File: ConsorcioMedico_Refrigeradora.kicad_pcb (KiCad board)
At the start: 2 copper layers, 260 x 70 mm, 156 parts, among them J1 BatteryHolder, J10 AC, J11 Digital, J12 Light, J13 Light, J14 Compress, J15 Resistor, J16 Analog, J18 Resistor, J19 AC, J2 USART, J3 USART, J4 SWD, J5 Evap_fan, J6 Screw_Terminal_01x01, J7 Screw_Terminal_01x01, J8 Evap_fan, J9 Compress, K1 HF46F-G/012-HS1T, K2 AZ2150-1A-12DEF, K3 HF46F-G/012-HS1T, K4 HF46F-G/012-HS1T, Q1 MMBT3904, Q11 BSS806, Q2 MMBT3904, Q3 MMBT3904, Q4 MMBT3904, Q5 BSS806, Q6 BSS806, Q7 BSS806, Q8 BSS806, Q9 BSS806, U1 STM32F411RETx, U2 AP63205WU, U3 LDL1117, U4 INA350, U5 INA350, U6 LTV-357T, U7 LTV-357T, U9 HLK-PMx, Y1 8Mhz, Y2 32.768khz/12.5pF

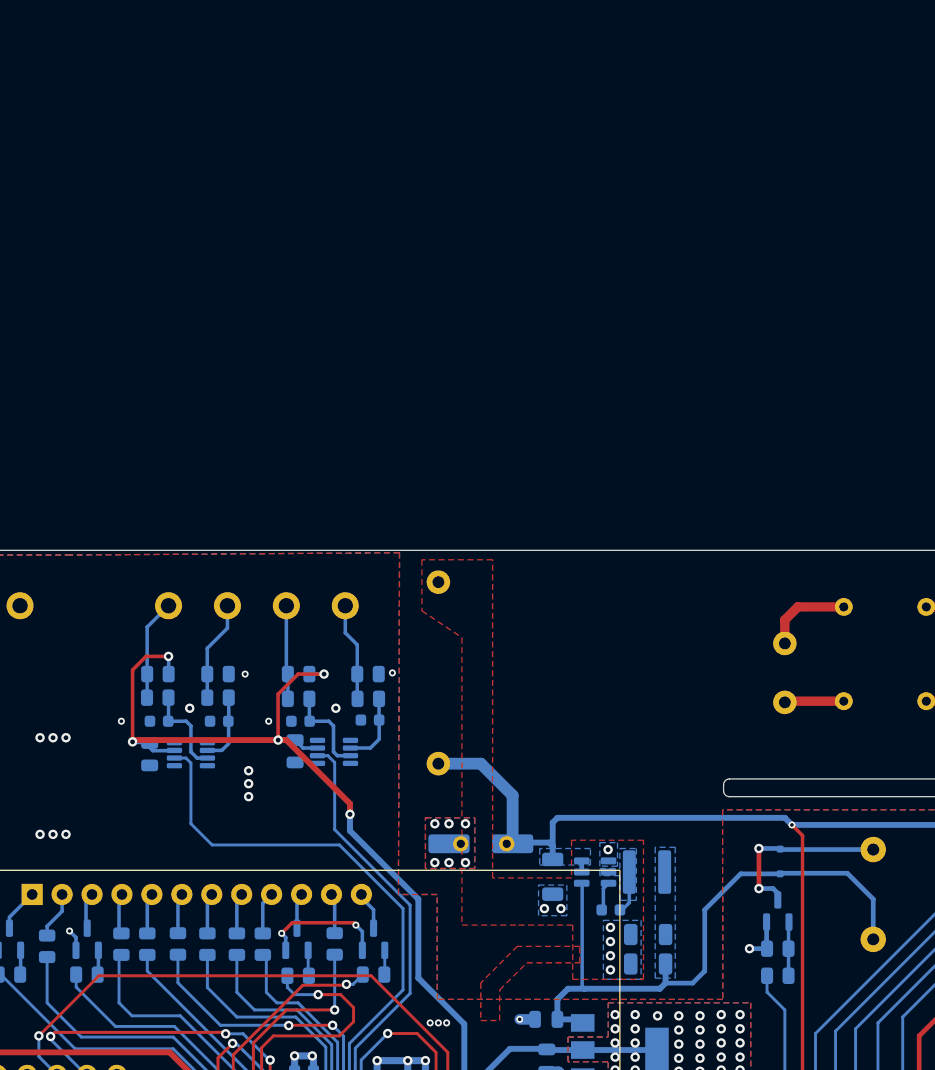
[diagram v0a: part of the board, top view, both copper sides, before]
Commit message: SCH:Se modifica los leds y nombres, en este punto, posibilemente se cambie el tamaño de la placa
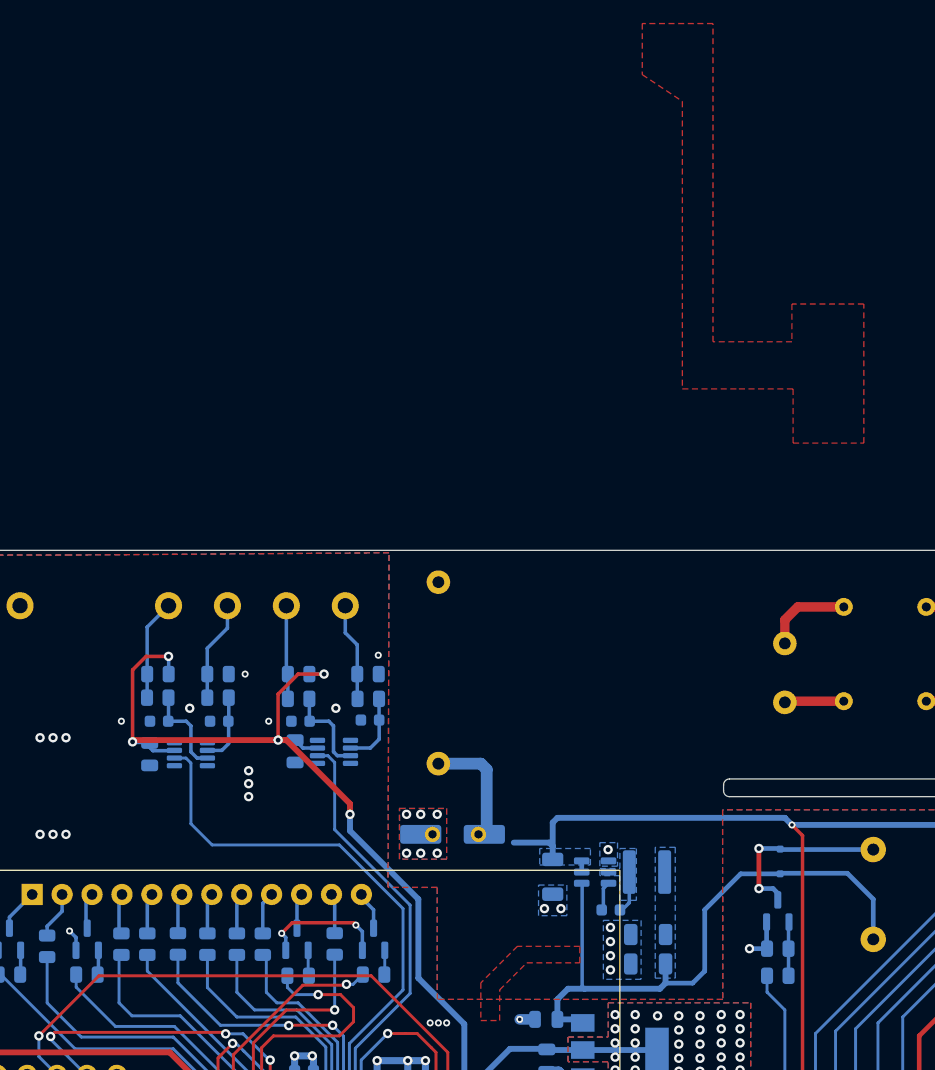
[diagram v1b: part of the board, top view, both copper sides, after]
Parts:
- moved J6 2.53 mm to (78.6, 87.7)
- moved C29 2.53 mm to (76.4, 87.7)
- moved J7 2.53 mm to (74.7, 87.7)
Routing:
- net +12V: track 410.1 -> 408.4 mm
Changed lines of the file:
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@@
   )
   (footprint "1-Pad:Pad_0.7mm_1.3mm" (layer "F.Cu")
-    (at 77.1 88.5)
+    (at 74.7 87.7)
     (property "Sheetfile" "ConsorcioMedico_Refrigeradora.kicad_sch")
     (property "Sheetname" "")
@@
   )
   (footprint "1-Pad:Pad_0.7mm_1.3mm" (layer "F.Cu")
-    (at 81 88.5)
+    (at 78.6 87.7)
     (property "Sheetfile" "ConsorcioMedico_Refrigeradora.kicad_sch")
     (property "Sheetname" "")
@@
   )
   (footprint "Capacitor_SMD:CP_Elec_6.3x7.7" (layer "B.Cu")
-    (at 78.8 88.5 180)
+    (at 76.4 87.7 180)
     (descr "SMD capacitor, aluminum electrolytic, Nichicon, 6.3x7.7mm")
     (tags "capacitor electrolytic")
@@
   (via (at 89.8 98) (size 0.8) (drill 0.4) (layers "F.Cu" "B.Cu") (net 2))
   (via (at 72.6 106.9) (size 0.8) (drill 0.4) (layers "F.Cu" "B.Cu") (net 2))
-  (via (at 77.5 90.1) (size 0.8) (drill 0.4) (layers "F.Cu" "B.Cu") (net 2))
+  (via (at 75.1 89.3) (size 0.8) (drill 0.4) (layers "F.Cu" "B.Cu") (net 2))
   (via (at 52.4 117.6) (size 0.6) (drill 0.3) (layers "F.Cu" "B.Cu") (net 2))
   (via (at 67.5 116.6) (size 0.6) (drill 0.3) (layers "F.Cu" "B.Cu") (net 2))
@@
   (via (at 174.6 83.4) (size 0.8) (drill 0.4) (layers "F.Cu" "B.Cu") (free) (net 2))
   (via (at 89.8 95.6) (size 0.8) (drill 0.4) (layers "F.Cu" "B.Cu") (net 2))
-  (via (at 74.9 90.1) (size 0.8) (drill 0.4) (layers "F.Cu" "B.Cu") (net 2))
+  (via (at 72.5 89.3) (size 0.8) (drill 0.4) (layers "F.Cu" "B.Cu") (net 2))
   (via (at 146.5 83.3) (size 0.8) (drill 0.4) (layers "F.Cu" "B.Cu") (free) (net 2))
-  (via (at 76.1 90.1) (size 0.8) (drill 0.4) (layers "F.Cu" "B.Cu") (net 2))
+  (via (at 73.7 89.3) (size 0.8) (drill 0.4) (layers "F.Cu" "B.Cu") (net 2))
   (via (at 122.6 126.1) (size 0.8) (drill 0.4) (layers "F.Cu" "B.Cu") (free) (net 2))
   (via (at 74.5 103.7) (size 0.6) (drill 0.3) (layers "F.Cu" "B.Cu") (free) (net 2))
@@
   (via (at 89.8 96.8) (size 0.8) (drill 0.4) (layers "F.Cu" "B.Cu") (net 2))
   (via (at 59.1 84.5) (size 0.8) (drill 0.4) (layers "F.Cu" "B.Cu") (free) (net 2))
-  (via (at 74.9 86.8) (size 0.8) (drill 0.4) (layers "F.Cu" "B.Cu") (net 2))
+  (via (at 72.5 86) (size 0.8) (drill 0.4) (layers "F.Cu" "B.Cu") (net 2))
   (via (at 63.1 110.3) (size 0.6) (drill 0.3) (layers "F.Cu" "B.Cu") (net 2))
   (via (at 75.2 103.7) (size 0.6) (drill 0.3) (layers "F.Cu" "B.Cu") (free) (net 2))
@@
   (via (at 80.9 127.5) (size 0.6) (drill 0.3) (layers "F.Cu" "B.Cu") (free) (net 2))
   (via (at 85.6 94) (size 0.8) (drill 0.4) (layers "F.Cu" "B.Cu") (net 2))
-  (via (at 71.3 74) (size 0.6) (drill 0.3) (layers "F.Cu" "B.Cu") (free) (net 2))
+  (via (at 70.1 72.5) (size 0.6) (drill 0.3) (layers "F.Cu" "B.Cu") (free) (net 2))
   (via (at 89.8 99.2) (size 0.8) (drill 0.4) (layers "F.Cu" "B.Cu") (net 2))
   (via (at 16.6 83.4) (size 0.8) (drill 0.4) (layers "F.Cu" "B.Cu") (free) (net 2))
@@
   (via (at 170.4 83.4) (size 0.8) (drill 0.4) (layers "F.Cu" "B.Cu") (free) (net 2))
   (via (at 212.2 83.3) (size 0.8) (drill 0.4) (layers "F.Cu" "B.Cu") (free) (net 2))
-  (via (at 76.1 86.8) (size 0.8) (drill 0.4) (layers "F.Cu" "B.Cu") (net 2))
+  (via (at 73.7 86) (size 0.8) (drill 0.4) (layers "F.Cu" "B.Cu") (net 2))
   (via (at 123.7 126.1) (size 0.8) (drill 0.4) (layers "F.Cu" "B.Cu") (free) (net 2))
   (via (at 54.1 77) (size 0.8) (drill 0.4) (layers "F.Cu" "B.Cu") (free) (net 2))
@@
   (via (at 132.5 114.6) (size 0.8) (drill 0.4) (layers "F.Cu" "B.Cu") (free) (net 2))
   (via (at 64.5 106.5) (size 0.8) (drill 0.4) (layers "F.Cu" "B.Cu") (net 2))
-  (via (at 77.5 86.8) (size 0.8) (drill 0.4) (layers "F.Cu" "B.Cu") (net 2))
+  (via (at 75.1 86) (size 0.8) (drill 0.4) (layers "F.Cu" "B.Cu") (net 2))
   (via (at 80.9 125.5) (size 0.6) (drill 0.3) (layers "F.Cu" "B.Cu") (free) (net 2))
   (via (at 59.1 83.4) (size 0.8) (drill 0.4) (layers "F.Cu" "B.Cu") (free) (net 2))
@@
   (via (at 166.5 86.5) (size 0.8) (drill 0.4) (layers "F.Cu" "B.Cu") (net 106))
   (segment (start 204.95 86.3) (end 204.95 84.45) (width 0.5) (layer "B.Cu") (net 106))
-  (segment (start 81.5 88.5) (end 81.5 84.4) (width 1) (layer "B.Cu") (net 106))
   (segment (start 204.95 84.45) (end 206.05 83.35) (width 0.5) (layer "B.Cu") (net 106))
   (segment (start 87.3625 90.9) (end 87.3625 89.95) (width 0.4) (layer "B.Cu") (net 106))
@@
   (segment (start 186.0875 86.0875) (end 186.5 86.5) (width 0.5) (layer "B.Cu") (net 106))
   (segment (start 218.35 88.95) (end 220.7 86.6) (width 0.5) (layer "B.Cu") (net 106))
-  (segment (start 81.5 84.4) (end 78.8 81.7) (width 1) (layer "B.Cu") (net 106))
   (segment (start 220.7 84.9) (end 222.235 83.365) (width 0.5) (layer "B.Cu") (net 106))
   (segment (start 105.2 86.9) (end 104.6 86.3) (width 0.5) (layer "B.Cu") (net 106))
@@
   (segment (start 165.05 85.05) (end 166.35 83.75) (width 0.5) (layer "B.Cu") (net 106))
   (segment (start 220.7 86.6) (end 220.7 84.9) (width 0.5) (layer "B.Cu") (net 106))
+  (segment (start 79.3 87.7) (end 79.3 82.2) (width 1) (layer "B.Cu") (net 106))
   (segment (start 186.25 83.35) (end 186.65 83.35) (width 0.5) (layer "B.Cu") (net 106))
   (segment (start 206 86.3) (end 206.2 86.5) (width 0.5) (layer "B.Cu") (net 106))
@@
   (segment (start 165.05 86.1125) (end 165.05 85.05) (width 0.5) (layer "B.Cu") (net 106))
   (segment (start 165.05 86.1125) (end 166.1125 86.1125) (width 0.5) (layer "B.Cu") (net 106))
-  (segment (start 81.6 88.4) (end 81.5 88.5) (width 0.5) (layer "B.Cu") (net 106))
+  (segment (start 79.2 87.6) (end 79.1 87.7) (width 0.5) (layer "B.Cu") (net 106))
   (segment (start 21.8 72.4) (end 20.6 73.6) (width 0.3) (layer "B.Cu") (net 106))
+  (segment (start 79.3 82.2) (end 78.8 81.7) (width 1) (layer "B.Cu") (net 106))
   (segment (start 217.6 90) (end 217.5 90.1) (width 0.5) (layer "B.Cu") (net 106))
   (segment (start 32.1125 66.1125) (end 31.3 65.3) (width 0.3) (layer "B.Cu") (net 106))
@@
     (polygon
       (pts
-        (xy 73.8 64.4)
-        (xy 73.8 68.733334)
-        (xy 77.2 71)
-        (xy 77.2 95.4)
-        (xy 82 95.4)
-        (xy 86.6 95.4)
-        (xy 86.6 100)
-        (xy 92.6 100)
-        (xy 92.6 88.2)
-        (xy 86.5 88.2)
-        (xy 86.5 91.4)
-        (xy 79.8 91.4)
-        (xy 79.8 64.4)
+        (xy 92.5 18.9)
+        (xy 92.5 23.233334)
+        (xy 95.9 25.5)
+        (xy 95.9 49.9)
+        (xy 100.7 49.9)
+        (xy 105.3 49.9)
+        (xy 105.3 54.5)
+        (xy 111.3 54.5)
+        (xy 111.3 42.7)
+        (xy 105.2 42.7)
+        (xy 105.2 45.9)
+        (xy 98.5 45.9)
+        (xy 98.5 18.9)
       )
     )
@@
     (connect_pads (clearance 0.3))
     (min_thickness 0.25) (filled_areas_thickness no)
-    (fill yes (thermal_gap 0.5) (thermal_bridge_width 0.5) (smoothing fillet) (radius 0.5))
+    (fill (thermal_gap 0.5) (thermal_bridge_width 0.5) (smoothing fillet) (radius 0.5))
     (polygon
       (pts
@@
         (xy 99.326686 101.703776)
         (xy 75.1 101.7)
-        (xy 75.1 92.8)
-        (xy 71.810467 92.8)
-        (xy 71.9 63.8)
+        (xy 75.1 92.2)
+        (xy 70.925283 92.2)
+        (xy 71.012944 63.806359)
         (xy 44 64)
       )
@@
     (connect_pads yes (clearance 0.3))
     (min_thickness 0.25) (filled_areas_thickness no)
-    (fill yes (thermal_gap 0.5) (thermal_bridge_width 0.5) (smoothing fillet) (radius 0.25))
+    (fill (thermal_gap 0.5) (thermal_bridge_width 0.5) (smoothing fillet) (radius 0.25))
     (polygon
       (pts
-        (xy 74.1 86.3)
-        (xy 78.3 86.3)
-        (xy 78.3 90.6)
-        (xy 74.1 90.6)
+        (xy 71.9 85.5)
+        (xy 75.9 85.5)
+        (xy 75.9 89.8)
+        (xy 71.9 89.8)
       )
     )

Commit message: SCH
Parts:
- added D13: Button_Lock, 1-Led:LED_3mm, F.Cu at (108.9, 104.6)
- added D14: Door_State, 1-Led:LED_3mm, F.Cu at (108.9, 117.2)
- added D3: Powe_State, 1-Led:LED_3mm, F.Cu at (108.9, 91.9)
- added R52: 560R, 1-Resistor:R_0805_2012Metric, B.Cu at (108.8, 95.3)
- added R58: 560R, 1-Resistor:R_0805_2012Metric, B.Cu at (109.0, 107.9)
- added R59: 560R, 1-Resistor:R_0805_2012Metric, B.Cu at (109.0, 113.7)
- D7: value L-144IDT -> Cooling_State; footprint 1-Led:LED_3.9x1.9mm -> 1-Led:LED_3mm
- D8: value L-144IDT -> Defroting_State; footprint 1-Led:LED_3.9x1.9mm -> 1-Led:LED_3mm
- D9: value L-144IDT -> Fan_State; footprint 1-Led:LED_3.9x1.9mm -> 1-Led:LED_3mm
- J3: value USART -> I2C
- R2, R4, R5: value 330 -> 560R
- moved C12 25.4 mm to (45.2, 122.4), turned to -90 degrees
- moved R16 22.2 mm to (152.4, 113.5), turned to 180 degrees
- moved S2 19.7 mm to (153.4, 110.8)
- moved R17 18.5 mm to (179.2, 113.5), turned to 180 degrees
- moved J1 17.7 mm to (41.2, 122.3), turned to 180 degrees
- moved S3 16.5 mm to (180.3, 110.8)
- moved R18 14.8 mm to (198.3, 113.5), turned to 180 degrees
- moved S4 11.6 mm to (199.3, 110.8)
- moved SG2 11.0 mm to (122.8, 95.5), turned to 90 degrees
- moved Q11 10.8 mm to (114.7, 95.5)
- moved R56 10.8 mm to (114.7, 101.0)
- moved R57 10.8 mm to (114.7, 98.7)
- moved D2 10.7 mm to (114.8, 91.5), turned to -90 degrees
- moved R15 9.48 mm to (217.8, 113.5), turned to 180 degrees
- moved R5 7.31 mm to (10.9, 120.5)
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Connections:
- net Button_Buzzer renamed Button_Power
- net Button_Touch renamed Button_Set
- net LED_Defrost renamed Led_Cooling_State
- net LED_Door renamed Led_Defroting_State
- net LED_Status renamed Led_Status
- net LED_TempAlarm renamed Led_Fan_State
- R19 pad 1: Button_Cooling -> Button_Light
- R20 pad 1: Button_Light -> Button_Sound
- S5 pad 1: Button_Cooling -> Button_Light
- S6 pad 1: Button_Light -> Button_Sound
- U1 pad 27: unconnected-(U1-PB1-Pad27) -> Led_Power_State
- U1 pad 28: unconnected-(U1-PB2-Pad28) -> Led_Button_Lock
- U1 pad 29: unconnected-(U1-PB10-Pad29) -> Led_Door_State
- U1 pad 53: Button_Cooling -> Button_Light
- U1 pad 54: Button_Light -> Button_Sound
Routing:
- net GND: track 465.7 -> 116.0 mm, vias 104 -> 124
- net Button_Sound: track 0.00 -> 213.8 mm
- net Button_Cooling: track 187.6 -> 0.00 mm
- net +12V: track 408.4 -> 336.3 mm, vias 9 -> 8
- net Led_Power_State: track 0.00 -> 69.4 mm, vias 0 -> 2
- net Led_Button_Lock: track 0.00 -> 59.1 mm, vias 0 -> 2
- net Led_Door_State: track 0.00 -> 58.1 mm, vias 0 -> 2
- net Button_Light: track 217.4 -> 186.4 mm
- net +BATT: track 58.8 -> 31.3 mm, vias 2 -> 0
- net +3.3V: track 495.9 -> 518.4 mm, vias 57 -> 52
- net Button_Power: track 69.1 -> 89.1 mm
- net Button_Set: track 100.2 -> 117.0 mm
- net SWDIO: track 59.0 -> 74.9 mm
- net +5V: track 53.2 -> 69.1 mm
- net Led_Cooling_State: track 71.2 -> 84.3 mm
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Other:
- board size 260 x 70 mm -> 265 x 70 mm
- board text added: "Bridge_Controller_V2"
- board text added: "POWER"
- board text added: "SET"
- board text added: "SOUND"
- board text removed: "BUZZER"
- board text removed: "COOLING"
- board text removed: "TOUCH"

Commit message: Luego de modificaciones de Dandy
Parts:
- added C13: 100nF 50V, 1-Capacitor:C_0603_1608Metric, B.Cu at (79.7, 107.4)
- added C34: 100nF 50V, 1-Capacitor:C_0603_1608Metric, B.Cu at (82.1, 89.3)
- added C35: 1uF 50V, 1-Capacitor:C_0805_2012Metric, F.Cu at (87.5, 137.2)
- added JP3: SolderJumper_3_Open, 1-Jumper:SolderJumper-3_P1.3mm_Open_RoundedPad1.0x1.5mm, F.Cu at (25.4, 68.2)
- added R60: 10k, 1-Resistor:R_0805_2012Metric, B.Cu at (45.6, 76.6)
- added R61: 910R, 1-Resistor:R_0805_2012Metric, B.Cu at (49.9, 76.6)
- added R62: 10k, 1-Resistor:R_0805_2012Metric, B.Cu at (58.0, 76.6)
- added R63: 910R, 1-Resistor:R_0805_2012Metric, B.Cu at (62.3, 76.6)
- added R64: 1k, 1-Resistor:R_0805_2012Metric, F.Cu at (87.5, 140.2)
- C14: value 1uF 10V -> 100nF 50V; footprint 1-Capacitor:C_0805_2012Metric -> 1-Capacitor:C_0603_1608Metric
- R15: value 10k -> 22k
- R21, R26: value 3.9k -> 10k
- R25, R30: value 2.7k -> 1k
- moved C31 5.24 mm to (85.3, 88.5), turned to 0 degrees
- moved C24 4.35 mm to (56.7, 84.9)
- moved C21 4.10 mm to (44.3, 84.9)
- moved U5 3.70 mm to (60.1, 84.3)
- moved U4 3.50 mm to (47.7, 84.3)
- moved D2 3.06 mm to (114.6, 94.6)
- moved Q11 3.06 mm to (114.6, 98.6)
- moved R56 3.06 mm to (114.6, 104.1)
- moved R57 3.06 mm to (114.6, 101.8)
- moved C25 2.98 mm to (62.3, 80.8)
- moved C26 2.94 mm to (58.0, 80.8)
- moved R27 2.91 mm to (58.0, 78.8)
- moved R22 2.87 mm to (45.6, 78.8)
- moved C23 2.85 mm to (45.6, 80.8)
- moved C22 2.81 mm to (49.9, 80.8)
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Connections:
- J11 pad 2: GND -> Net-(J11-Pin_2)
- J11 pad 4: GND -> Net-(J11-Pin_2)
- R15 pad 1: Button_Down -> Net-(R15-Pad1)
- R23 pad 1: Net-(J16-Pin_2) -> Net-(R23-Pad1)
- R28 pad 1: Net-(J16-Pin_4) -> Net-(R28-Pad1)
- S1 pad 1: Button_Down -> Net-(R15-Pad1)
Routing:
- net +12V: track 336.3 -> 287.7 mm, vias 8 -> 7
- net GND: track 116.0 -> 91.0 mm, vias 124 -> 159
- net +3.3V: track 518.4 -> 536.8 mm, vias 52 -> 48
- net Net-(J11-Pin_2): track 0.00 -> 14.1 mm
- net Relay_Compressor_Save: track 156.2 -> 161.9 mm
- net Net-(J16-Pin_3): track 7.95 -> 13.0 mm
- net Net-(J16-Pin_1): track 8.56 -> 13.3 mm
- net Net-(R28-Pad1): track 0.00 -> 4.68 mm
- net Net-(R23-Pad1): track 0.00 -> 4.67 mm
- net RTD2: track 36.2 -> 32.1 mm
- net Relay_Fan: track 145.5 -> 148.9 mm
- net Relay_Compressor: track 159.6 -> 162.9 mm
- net Relay_Calefac: track 125.4 -> 128.6 mm
- net RTD1: track 46.8 -> 43.8 mm
- net Net-(D2-A): track 14.4 -> 11.7 mm
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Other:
- board text added: "+"
- board text added: "-"
- board text removed: "Bridge_Controller_V2"
